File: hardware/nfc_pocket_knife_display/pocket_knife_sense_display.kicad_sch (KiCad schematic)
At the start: 17 parts, among them U1 TMP117AIDRVR, U3 ATtiny1626-MFR

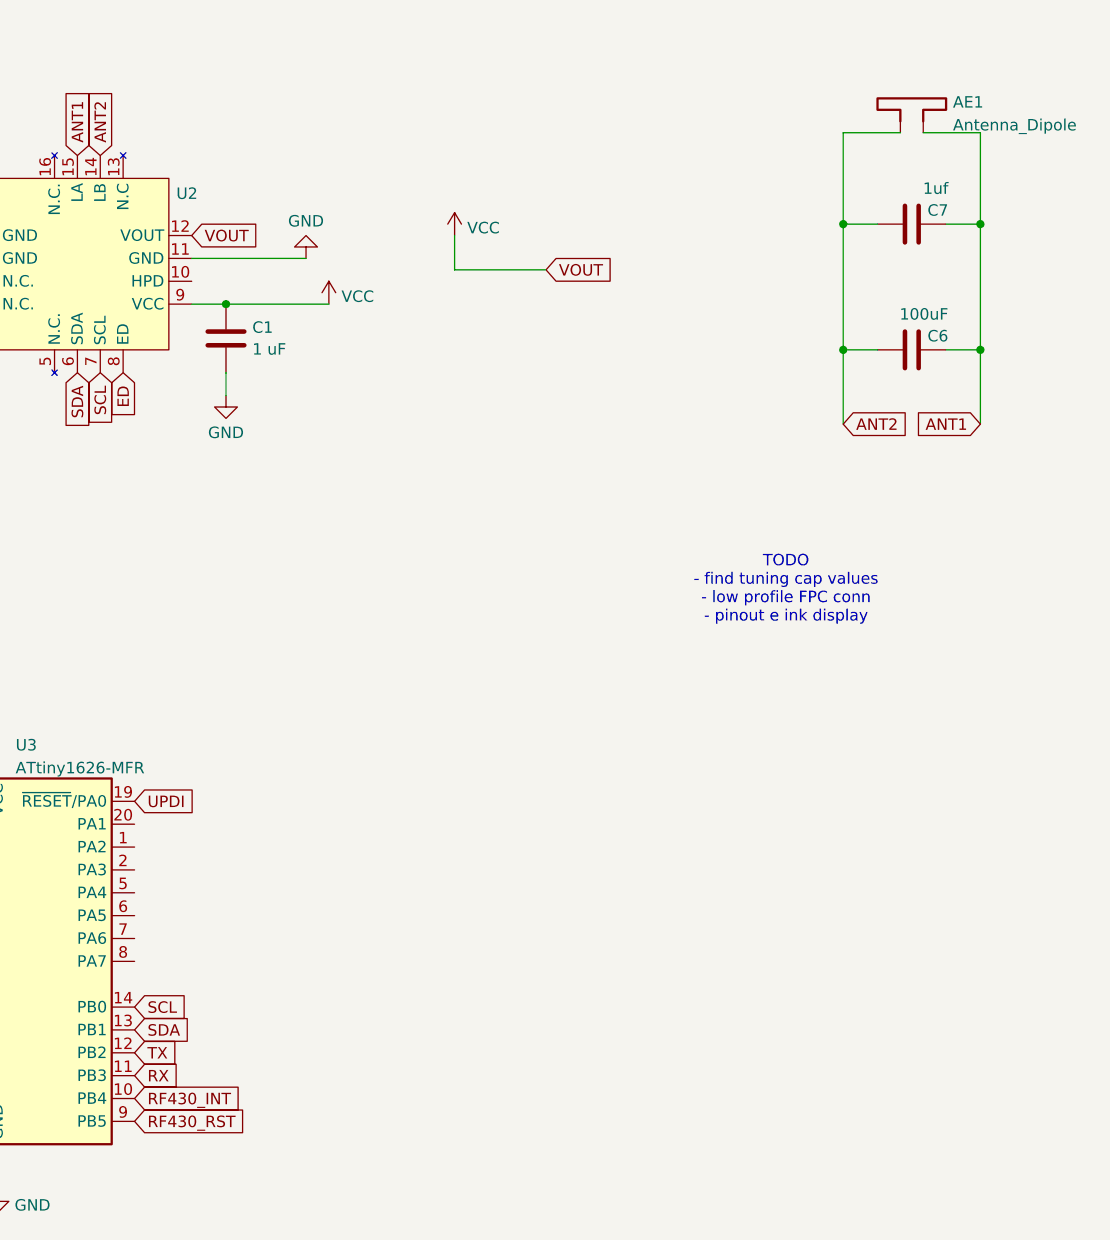
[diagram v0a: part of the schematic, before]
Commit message: preparation for e ink display via FPC
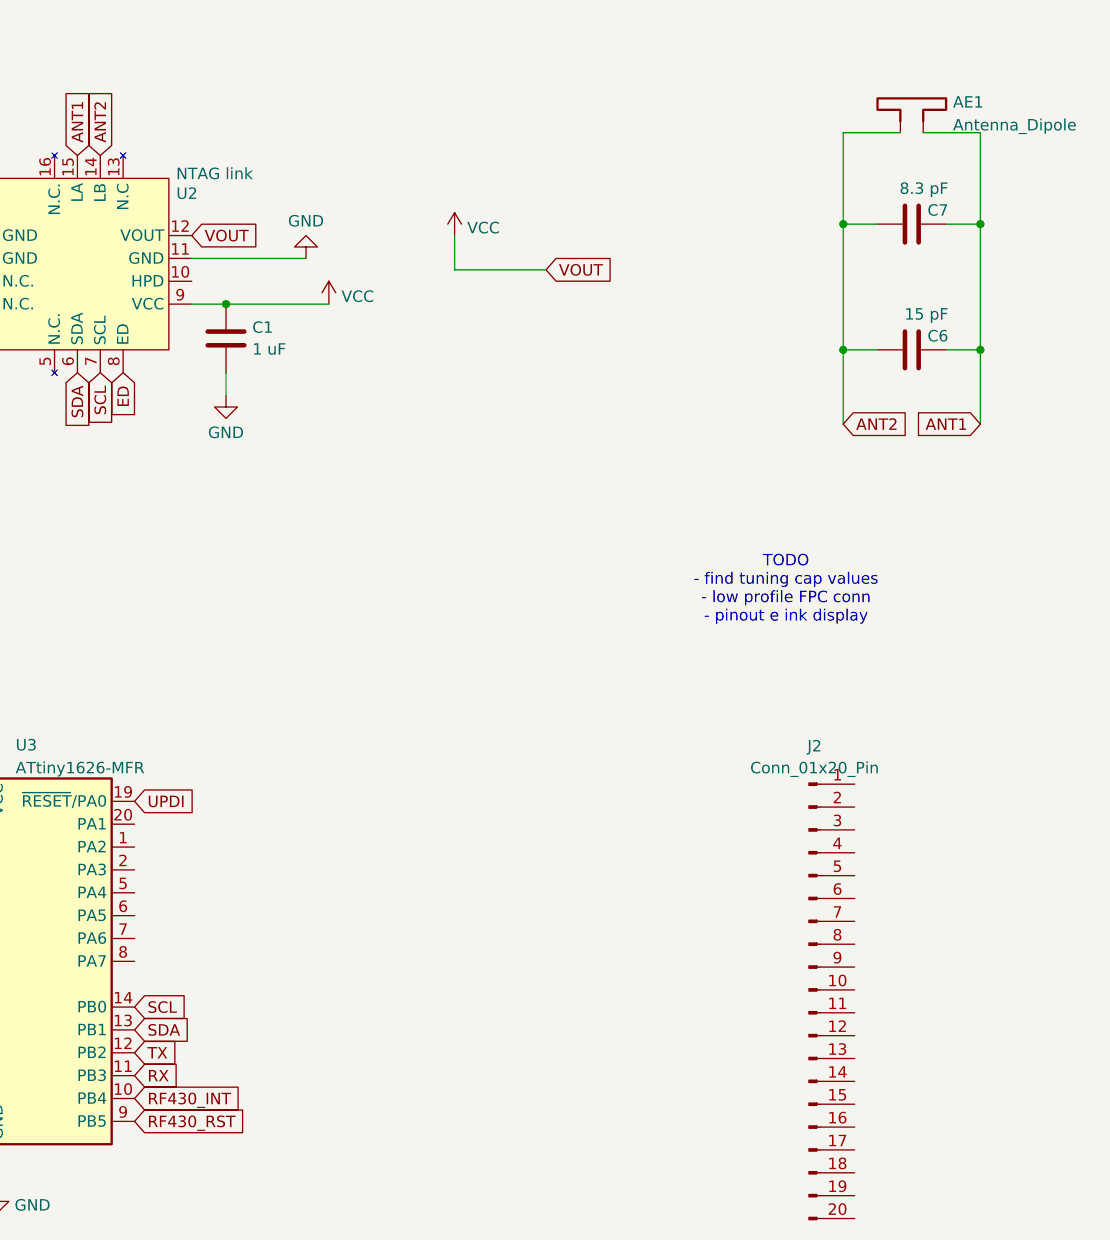
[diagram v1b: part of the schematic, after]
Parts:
- added J2: Conn_01x20_Pin, unsurv_offline_pcb_footprints:FH34SRJ-18S-0.5SH, symbol Connector:Conn_01x20_Pin
- C6: value 100uF -> 15 pF
- C7: value 1uf -> 8.3 pF
- D1: footprint (none) -> LED_SMD:LED_0603_1608Metric
- U2: value ~ -> NTAG link; footprint (none) -> unsurv_offline_pcb_footprints:NTAG 5 link
- U4: footprint (none) -> unsurv_offline_pcb_footprints:testpoint_array_2x3
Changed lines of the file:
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@@
+	)
+	(symbol
+		(lib_id "Connector:Conn_01x20_Pin")
+		(at 154.94 134.62 0)
+		(unit 1)
+		(exclude_from_sim no)
+		(in_bom yes)
+		(on_board yes)
+		(dnp no)
+		(fields_autoplaced yes)
+		(property "Reference" "J2"
+			(at 155.575 107.5393 0)
+			(effects
+				(font
+					(size 1.27 1.27)
+				)
+			)
+		)
+		(property "Value" "Conn_01x20_Pin"
+			(at 155.575 109.9636 0)
+			(effects
+				(font
+					(size 1.27 1.27)
+				)
+			)
+		)
+		(property "Footprint" "unsurv_offline_pcb_footprints:FH34SRJ-18S-0.5SH"
+			(at 154.94 134.62 0)
+			(effects
+				(font
+					(size 1.27 1.27)
+				)
+				(hide yes)
+			)
+		)
+		(property "Datasheet" "~"
+			(at 154.94 134.62 0)
+			(effects
+				(font
+					(size 1.27 1.27)
+				)
+				(hide yes)
+			)
+		)
+		(property "Description" "Generic connector, single row, 01x20, script generated"
+			(at 154.94 134.62 0)
+			(effects
+				(font
+					(size 1.27 1.27)
+				)
+				(hide yes)
+			)
+		)
+		(pin "10"
+		)
+		(pin "13"
+		)
+		(pin "3"
+		)
+		(pin "2"
+		)
+		(pin "17"
+		)
+		(pin "1"
+		)
+		(pin "19"
+		)
+		(pin "11"
+		)
+		(pin "12"
+		)
+		(pin "16"
+		)
+		(pin "4"
+		)
+		(pin "5"
+		)
+		(pin "9"
+		)
+		(pin "14"
+		)
+		(pin "15"
+		)
+		(pin "18"
+		)
+		(pin "20"
+		)
+		(pin "7"
+		)
+		(pin "8"
+		)
+		(pin "6"
+		)
+		(instances
+			(project ""
+				(path "/c54e1377-ff88-4224-9c85-352a20bf3450"
+					(reference "J2")
+					(unit 1)
+				)
+			)
+		)
 	)
 	(symbol
@@
 			)
 		)
-		(property "Value" "100uF"
+		(property "Value" "15 pF"
 			(at 170.434 59.5517 90)
 			(effects
@@
 			)
 		)
-		(property "Footprint" ""
+		(property "Footprint" "unsurv_offline_pcb_footprints:testpoint_array_2x3"
 			(at 219.71 115.57 0)
 			(effects
@@
 		(on_board yes)
 		(dnp no)
-		(fields_autoplaced yes)
 		(property "Reference" "U2"
 			(at 85.8362 46.1409 0)
@@
 			)
 		)
-		(property "Value" "~"
-			(at 85.8362 47.8223 0)
-			(effects
-				(font
-					(size 1.27 1.27)
-				)
-			)
-		)
-		(property "Footprint" ""
+		(property "Value" "NTAG link"
+			(at 88.9 43.942 0)
+			(effects
+				(font
+					(size 1.27 1.27)
+				)
+			)
+		)
+		(property "Footprint" "unsurv_offline_pcb_footprints:NTAG 5 link"
 			(at 71.12 58.42 0)
 			(effects
@@
 			)
 		)
-		(property "Value" "1uf"
+		(property "Value" "8.3 pF"
 			(at 170.434 45.5817 90)
 			(effects
@@
 			)
 		)
-		(property "Footprint" ""
+		(property "Footprint" "LED_SMD:LED_0603_1608Metric"
 			(at 52.07 78.74 0)
 			(effects

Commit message: add surface temperature version
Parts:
- removed U4: ~, unsurv_offline_pcb_footprints:testpoint_array_2x3, symbol unsurv_offline_pcb_symbols:testpoint_array_2x3
- added C10, C2, C4, C5, C9: 1 uF 25 V, Capacitor_SMD:C_0402_1005Metric, symbol Device:C
- added C11, C12: 4.7uF, Capacitor_SMD:C_0402_1005Metric, symbol Device:C
- added C13: 1uF, Capacitor_SMD:C_0402_1005Metric, symbol Device:C
- added D2, D3, D4: MBR0530, Diode_SMD:D_SOD-123, symbol Diode:MBR0530
- added L1: 47uH 500mA, Inductor_SMD:L_Taiyo-Yuden_MD-3030, symbol Device:L
- added Q1: Si1308EDL, Package_TO_SOT_SMD:SOT-323_SC-70, symbol Transistor_FET:Si1308EDL
- added R4: 2.2, Resistor_SMD:R_0402_1005Metric, symbol Device:R
- added R5: 10k, Resistor_SMD:R_0402_1005Metric, symbol Device:R
- added TP1, TP2, TP3, TP6, TP7: TestPoint, TestPoint:TestPoint_Pad_D1.0mm, symbol Connector:TestPoint
- C1, C6, C7, C8: footprint Capacitor_SMD:C_0603_1608Metric -> Capacitor_SMD:C_0402_1005Metric
- R1, R2: footprint Resistor_SMD:R_0603_1608Metric -> Resistor_SMD:R_0402_1005Metric
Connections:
- net ANT1: now also U2.14 (LB); no longer U2.15 (LA)
- net ANT2: now also U2.15 (LA); no longer U2.14 (LB)
- net GND: now also J2.11 (Pin_11), J2.19 (Pin_19), J2.20 (Pin_20), C10.1, C12.1, C13.1, C2.1, C4.1, C5.1, C9.1, D3.1 (K), R4.2, R5.2, TP3.1, TP7.1
- net RX: now also TP1.1
- net TX: now also TP2.1
- net UPDI: now also TP6.1
- net VCC: now also J2.10 (Pin_10), C12.2, L1.1
- net GDR: now reaches J2.1 (Pin_1)
- net GDR: now also Q1.1 (G), R5.1
- net at J2.12 (Pin_12): now also C9.2
- net at J2.14 (Pin_14): now also C5.2
- net PREVGH: now reaches J2.15 (Pin_15)
- net PREVGH: now also C13.2, D2.1 (K)
- net at J2.16 (Pin_16): now also C4.2
- net PREVGL: now reaches J2.17 (Pin_17)
- net PREVGL: now also D4.2 (A)
- net at J2.18 (Pin_18): now also C2.2
- net RESE: now reaches J2.2 (Pin_2)
- net RESE: now also Q1.2 (S), R4.1
- net at J2.3 (Pin_3): now also C10.2
- net BUSY: now reaches J2.4 (Pin_4)
- net RES: now reaches J2.5 (Pin_5)
- net D/C: now reaches J2.6 (Pin_6)
- net CS: now reaches J2.7 (Pin_7)
- net SCLK: now reaches J2.8 (Pin_8)
- net SDI: now reaches J2.9 (Pin_9)
- new net: C11.1, D2.2 (A), L1.2, Q1.3 (D)
- new net: C11.2, D3.2 (A), D4.1 (K)
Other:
- note added: "TODO - connect SPI for display"
- note removed: "TODO - find tuning cap values - low profile FPC conn - pinout e ink display"
- moved on the sheet: J2, TP5
